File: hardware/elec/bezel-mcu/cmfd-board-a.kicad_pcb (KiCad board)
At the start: 2 copper layers, 140 x 140 mm, 37 parts, among them J1 B2B, J2 SWD, SW1 GAIN, SW2 SYM, SW3 BRT, SW4 CON, U1 STM32G431CBU6, U4 AMS1117-3.3

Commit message: feat(hardware): route Board A OSB 4x5 matrix to MCU
Add headless pcbnew matrix routing: ROW/COL nets, via-at-switch, B.Cu
buses, rocker nets, pin map. Export refreshed KiCad Gerbers and DRC.

Refs: #137
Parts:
- H1, H2, H3, H4: footprint MountingHole_3.2mm_M3_Pad -> MountingHole_3.2mm_M3
- moved H1 11.3 mm to (15.0, 15.0)
- moved H2 11.3 mm to (125.0, 15.0)
- moved H3 11.3 mm to (125.0, 125.0)
- moved H4 11.3 mm to (15.0, 125.0)
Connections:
- J1 pad 1: (no net) -> 3V3
- J1 pad 2: (no net) -> 3V3
- J1 pad 3: (no net) -> GND
- J1 pad 4: (no net) -> GND
- J1 pad 5: (no net) -> UART_TX
- J1 pad 6: (no net) -> UART_RX
- J2 pad 1: (no net) -> SWDIO
- J2 pad 2: (no net) -> SWCLK
- J2 pad 3: (no net) -> GND
- J2 pad 4: (no net) -> 3V3
- S1 pad 1: GND -> ROW_TOP
- S1 pad 2: GND -> COL0
- S10 pad 1: GND -> ROW_RIGHT
- S10 pad 2: GND -> COL4
- S11 pad 1: GND -> ROW_BOT
- S11 pad 2: GND -> COL4
- S12 pad 1: GND -> ROW_BOT
- S12 pad 2: GND -> COL3
- S13 pad 1: GND -> ROW_BOT
- S13 pad 2: GND -> COL2
- S14 pad 1: GND -> ROW_BOT
- S14 pad 2: GND -> COL1
- S15 pad 1: GND -> ROW_BOT
- S15 pad 2: GND -> COL0
- S16 pad 1: GND -> ROW_LEFT
- S16 pad 2: GND -> COL4
- S17 pad 1: GND -> ROW_LEFT
- S17 pad 2: GND -> COL3
- S18 pad 1: GND -> ROW_LEFT
- S18 pad 2: GND -> COL2
- S19 pad 1: GND -> ROW_LEFT
- S19 pad 2: GND -> COL1
- S2 pad 1: GND -> ROW_TOP
- S2 pad 2: GND -> COL1
- S20 pad 1: GND -> ROW_LEFT
- S20 pad 2: GND -> COL0
- S3 pad 1: GND -> ROW_TOP
- S3 pad 2: GND -> COL2
- S4 pad 1: GND -> ROW_TOP
- S4 pad 2: GND -> COL3
- S5 pad 1: GND -> ROW_TOP
- S5 pad 2: GND -> COL4
- S6 pad 1: GND -> ROW_RIGHT
- S6 pad 2: GND -> COL0
- S7 pad 1: GND -> ROW_RIGHT
- S7 pad 2: GND -> COL1
- S8 pad 1: GND -> ROW_RIGHT
- S8 pad 2: GND -> COL2
- S9 pad 1: GND -> ROW_RIGHT
- S9 pad 2: GND -> COL3
- SW1 pad 1: (no net) -> RK_GAIN
- SW1 pad 2: (no net) -> GND
- SW2 pad 1: (no net) -> RK_SYM
- SW2 pad 2: (no net) -> GND
- SW3 pad 1: (no net) -> RK_BRT
- SW3 pad 2: (no net) -> GND
- SW4 pad 1: (no net) -> RK_CON
- SW4 pad 2: (no net) -> GND
- U1 pad 10: (no net) -> ROW_TOP
- U1 pad 11: (no net) -> ROW_RIGHT
- U1 pad 12: (no net) -> ROW_BOT
- U1 pad 13: (no net) -> ROW_LEFT
- U1 pad 14: (no net) -> COL0
- U1 pad 15: (no net) -> COL1
- U1 pad 16: (no net) -> COL2
- U1 pad 17: (no net) -> COL3
- U1 pad 18: (no net) -> COL4
- U1 pad 19: (no net) -> RK_GAIN
- U1 pad 20: (no net) -> RK_SYM
- U1 pad 21: (no net) -> RK_BRT
- U1 pad 22: (no net) -> RK_CON
- U1 pad 29: (no net) -> UART_TX
- U1 pad 30: (no net) -> UART_RX
- U1 pad 34: (no net) -> SWDIO
- U1 pad 37: (no net) -> SWCLK
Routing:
- net COL0: track 0.00 -> 571.0 mm, vias 0 -> 5
- net COL1: track 0.00 -> 533.4 mm, vias 0 -> 5
- net COL2: track 0.00 -> 505.3 mm, vias 0 -> 5
- net COL3: track 0.00 -> 476.8 mm, vias 0 -> 5
- net COL4: track 0.00 -> 448.0 mm, vias 0 -> 5
- net RK_SYM: track 0.00 -> 349.7 mm, vias 0 -> 2
- net ROW_TOP: track 0.00 -> 348.0 mm, vias 0 -> 6
- net ROW_RIGHT: track 0.00 -> 332.2 mm, vias 0 -> 6
- net RK_CON: track 0.00 -> 250.8 mm, vias 0 -> 2
- net ROW_LEFT: track 0.00 -> 231.2 mm, vias 0 -> 6
- net RK_GAIN: track 0.00 -> 223.4 mm, vias 0 -> 2
- net ROW_BOT: track 0.00 -> 216.2 mm, vias 0 -> 6
- net RK_BRT: track 0.00 -> 125.0 mm, vias 0 -> 2
- net UART_RX: track 0.00 -> 53.2 mm
- net UART_TX: track 0.00 -> 50.2 mm
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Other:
- board text added: "MATRIX B.Cu bus + via-at-switch"

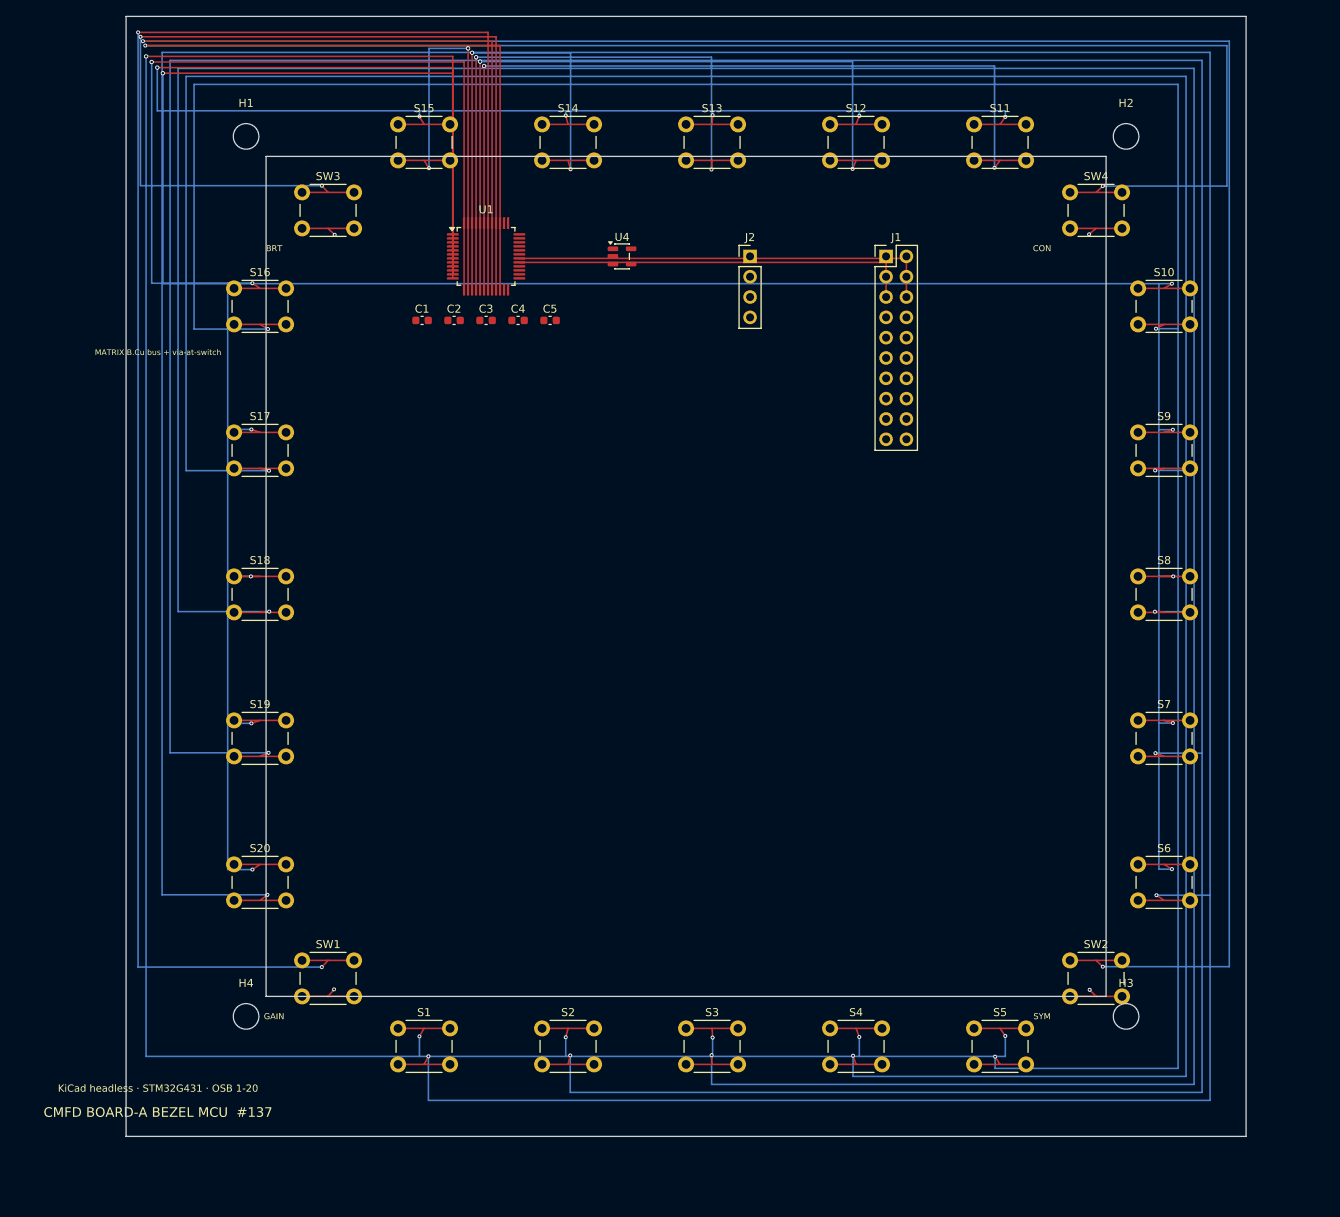
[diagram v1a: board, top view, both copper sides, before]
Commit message: feat(hardware): fab-ready passive bezel PCB + plain-language order guide
Board A is a switch-only panel: one pin per button, short tracks, zero
copper shorts on DRC. ORDER-THIS.md explains what to upload to JLCPCB and
the print shop with no KiCad steps.

Refs: #137
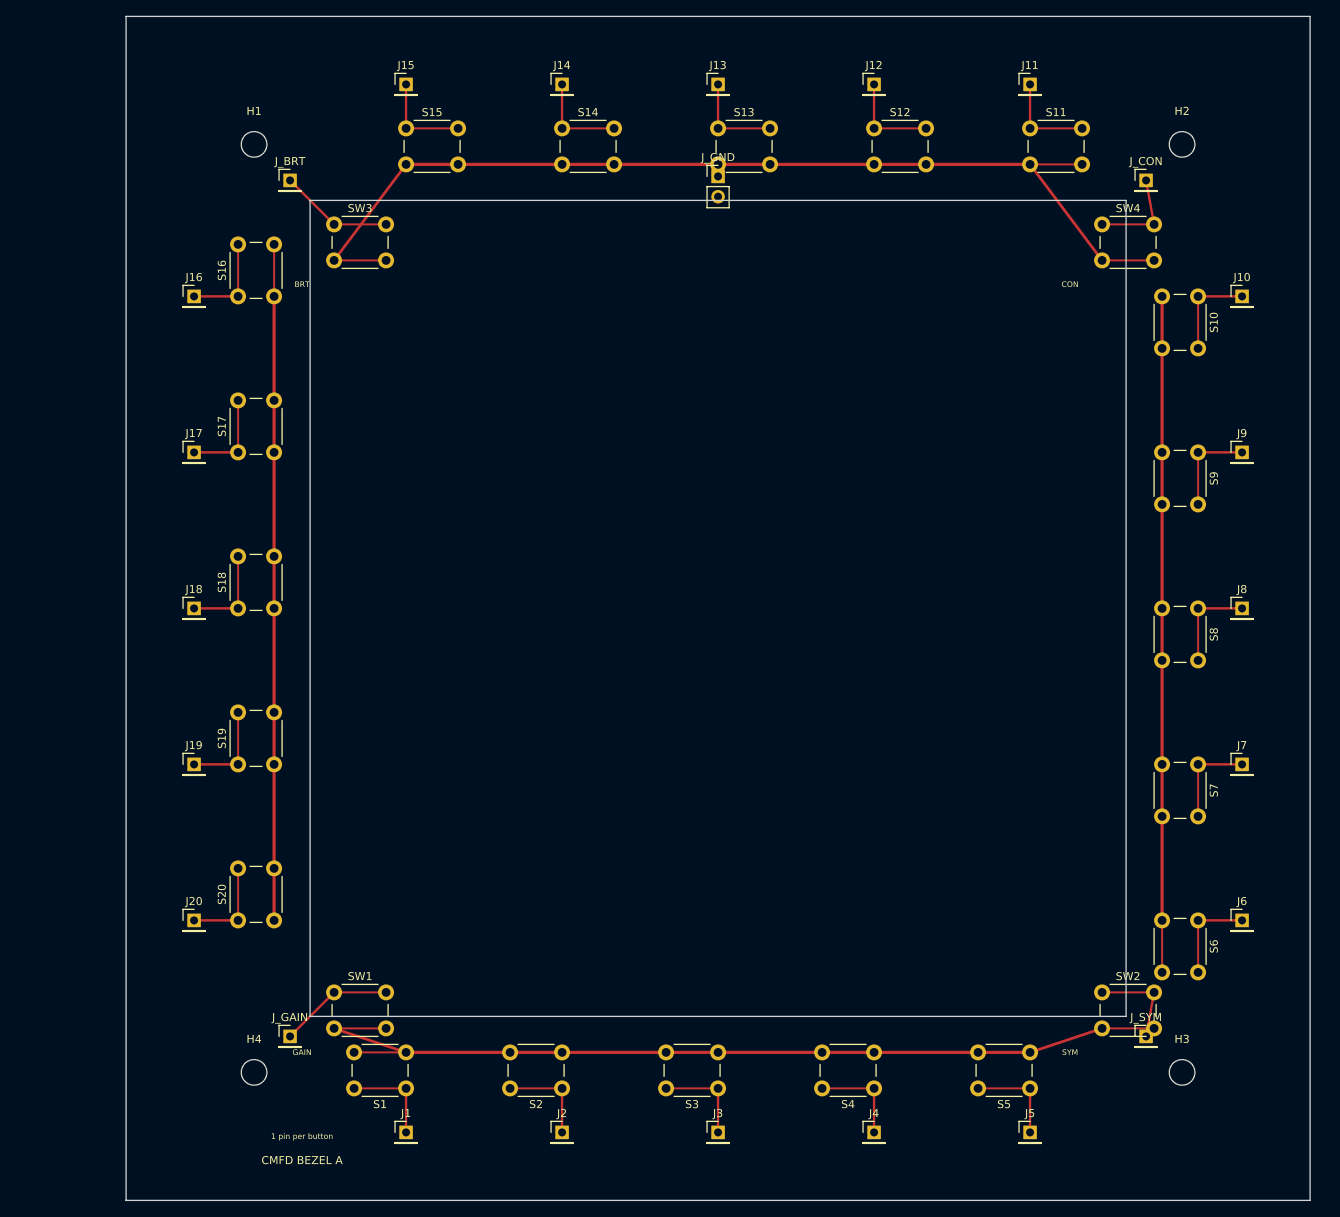
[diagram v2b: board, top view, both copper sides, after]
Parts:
- removed C1, C2, C3, C4, C5: 100nF, C_0603_1608Metric
- removed U1: STM32G431CBU6, LQFP-48_7x7mm_P0.5mm
- removed U4: AMS1117-3.3, SOT-23-5
- added J10: OSB10, PinHeader_1x01_P2.54mm_Vertical, F.Cu at (139.5, 35.0)
- added J11: OSB11, PinHeader_1x01_P2.54mm_Vertical, F.Cu at (113.0, 8.50)
- added J12: OSB12, PinHeader_1x01_P2.54mm_Vertical, F.Cu at (93.5, 8.50)
- added J13: OSB13, PinHeader_1x01_P2.54mm_Vertical, F.Cu at (74.0, 8.50)
- added J14: OSB14, PinHeader_1x01_P2.54mm_Vertical, F.Cu at (54.5, 8.50)
- added J15: OSB15, PinHeader_1x01_P2.54mm_Vertical, F.Cu at (35.0, 8.50)
- added J16: OSB16, PinHeader_1x01_P2.54mm_Vertical, F.Cu at (8.50, 35.0)
- added J17: OSB17, PinHeader_1x01_P2.54mm_Vertical, F.Cu at (8.50, 54.5)
- added J18: OSB18, PinHeader_1x01_P2.54mm_Vertical, F.Cu at (8.50, 74.0)
- added J19: OSB19, PinHeader_1x01_P2.54mm_Vertical, F.Cu at (8.50, 93.5)
- added J20: OSB20, PinHeader_1x01_P2.54mm_Vertical, F.Cu at (8.50, 113.0)
- added J3: OSB3, PinHeader_1x01_P2.54mm_Vertical, F.Cu at (74.0, 139.5)
- added J4: OSB4, PinHeader_1x01_P2.54mm_Vertical, F.Cu at (93.5, 139.5)
- added J5: OSB5, PinHeader_1x01_P2.54mm_Vertical, F.Cu at (113.0, 139.5)
- added J6: OSB6, PinHeader_1x01_P2.54mm_Vertical, F.Cu at (139.5, 113.0)
- added J7: OSB7, PinHeader_1x01_P2.54mm_Vertical, F.Cu at (139.5, 93.5)
- added J8: OSB8, PinHeader_1x01_P2.54mm_Vertical, F.Cu at (139.5, 74.0)
- added J9: OSB9, PinHeader_1x01_P2.54mm_Vertical, F.Cu at (139.5, 54.5)
- added J_BRT: BRT, PinHeader_1x01_P2.54mm_Vertical, F.Cu at (20.5, 20.5)
- added J_CON: CON, PinHeader_1x01_P2.54mm_Vertical, F.Cu at (127.5, 20.5)
- added J_GAIN: GAIN, PinHeader_1x01_P2.54mm_Vertical, F.Cu at (20.5, 127.5)
- added J_GND: GND, PinHeader_1x02_P2.54mm_Vertical, F.Cu at (74.0, 20.0)
- added J_SYM: SYM, PinHeader_1x01_P2.54mm_Vertical, F.Cu at (127.5, 127.5)
- J1: value B2B -> OSB1; footprint PinHeader_2x10_P2.54mm_Vertical -> PinHeader_1x01_P2.54mm_Vertical
- J2: value SWD -> OSB2; footprint PinHeader_1x04_P2.54mm_Vertical -> PinHeader_1x01_P2.54mm_Vertical
- moved J1 124.9 mm to (35.0, 139.5)
- moved J2 112.0 mm to (54.5, 139.5)
- moved S5 10.3 mm to (113.0, 134.0), turned to 180 degrees
- moved S6 10.3 mm to (134.0, 113.0), turned to -90 degrees
- moved H3 9.90 mm to (132.0, 132.0)
- moved S4 9.30 mm to (93.5, 134.0), turned to 180 degrees
- moved S7 9.30 mm to (134.0, 93.5), turned to -90 degrees
- moved S3 8.50 mm to (74.0, 134.0), turned to 180 degrees
- moved S8 8.50 mm to (134.0, 74.0), turned to -90 degrees
- moved S2 7.91 mm to (54.5, 134.0), turned to 180 degrees
- moved S9 7.91 mm to (134.0, 54.5), turned to -90 degrees
- moved S1 7.57 mm to (35.0, 134.0), turned to 180 degrees
- moved S10 7.57 mm to (134.0, 35.0), turned to -90 degrees
- moved H2 7.07 mm to (132.0, 16.0)
- moved H4 7.07 mm to (16.0, 132.0)
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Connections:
- J1 pad 1: 3V3 -> OSB1
- J2 pad 1: SWDIO -> OSB2
- S1 pad 1: ROW_TOP -> OSB1
- S1 pad 2: COL0 -> GND
- S10 pad 1: ROW_RIGHT -> OSB10
- S10 pad 2: COL4 -> GND
- S11 pad 1: ROW_BOT -> OSB11
- S11 pad 2: COL4 -> GND
- S12 pad 1: ROW_BOT -> OSB12
- S12 pad 2: COL3 -> GND
- S13 pad 1: ROW_BOT -> OSB13
- S13 pad 2: COL2 -> GND
- S14 pad 1: ROW_BOT -> OSB14
- S14 pad 2: COL1 -> GND
- S15 pad 1: ROW_BOT -> OSB15
- S15 pad 2: COL0 -> GND
- S16 pad 1: ROW_LEFT -> OSB16
- S16 pad 2: COL4 -> GND
- S17 pad 1: ROW_LEFT -> OSB17
- S17 pad 2: COL3 -> GND
- S18 pad 1: ROW_LEFT -> OSB18
- S18 pad 2: COL2 -> GND
- S19 pad 1: ROW_LEFT -> OSB19
- S19 pad 2: COL1 -> GND
- S2 pad 1: ROW_TOP -> OSB2
- S2 pad 2: COL1 -> GND
- S20 pad 1: ROW_LEFT -> OSB20
- S20 pad 2: COL0 -> GND
- S3 pad 1: ROW_TOP -> OSB3
- S3 pad 2: COL2 -> GND
- S4 pad 1: ROW_TOP -> OSB4
- S4 pad 2: COL3 -> GND
- S5 pad 1: ROW_TOP -> OSB5
- S5 pad 2: COL4 -> GND
- S6 pad 1: ROW_RIGHT -> OSB6
- S6 pad 2: COL0 -> GND
- S7 pad 1: ROW_RIGHT -> OSB7
- S7 pad 2: COL1 -> GND
- S8 pad 1: ROW_RIGHT -> OSB8
- S8 pad 2: COL2 -> GND
- S9 pad 1: ROW_RIGHT -> OSB9
- S9 pad 2: COL3 -> GND
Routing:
- net COL0: track 571.0 -> 0.00 mm, vias 5 -> 0
- net COL1: track 533.4 -> 0.00 mm, vias 5 -> 0
- net COL2: track 505.3 -> 0.00 mm, vias 5 -> 0
- net GND: track 30.6 -> 518.5 mm, vias 4 -> 0
- net COL3: track 476.8 -> 0.00 mm, vias 5 -> 0
- net COL4: track 448.0 -> 0.00 mm, vias 5 -> 0
- net ROW_TOP: track 348.0 -> 0.00 mm, vias 6 -> 0
- net RK_SYM: track 349.7 -> 12.1 mm, vias 2 -> 0
- net ROW_RIGHT: track 332.2 -> 0.00 mm, vias 6 -> 0
- net RK_CON: track 250.8 -> 12.1 mm, vias 2 -> 0
- net ROW_LEFT: track 231.2 -> 0.00 mm, vias 6 -> 0
- net ROW_BOT: track 216.2 -> 0.00 mm, vias 6 -> 0
- net RK_GAIN: track 223.4 -> 14.3 mm, vias 2 -> 0
- net RK_BRT: track 125.0 -> 14.3 mm, vias 2 -> 0
- net UART_RX: track 53.2 -> 0.00 mm
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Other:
- board size 140 x 140 mm -> 148 x 148 mm
- board text added: "1 pin per button"
- board text added: "CMFD BEZEL A"
- board text removed: "CMFD BOARD-A BEZEL MCU #137"
- board text removed: "KiCad headless · STM32G431 · OSB 1-20"
- board text removed: "MATRIX B.Cu bus + via-at-switch"

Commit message: fix(hardware): rockers clear glass, edge ports, M12, RA headers
- Rockers moved to pure corners (16 mm inset, 12×9 cap) so caps never
  enter the 102 mm glass aperture; OpenSCAD + KiCad + viewer aligned
- Board B USB-C / RJ45 / harness moved to front edge (not board center)
- Three M12 panel bulkheads on case left wall; J_M12 edge harness on B
- Board A uses right-angle 1-pin headers (outward); pins no longer
  taller than the 4.3 mm tact switches
- Rebuilt STLs, Gerbers, KiCad raytraces, Blender studio shots

Refs: #137
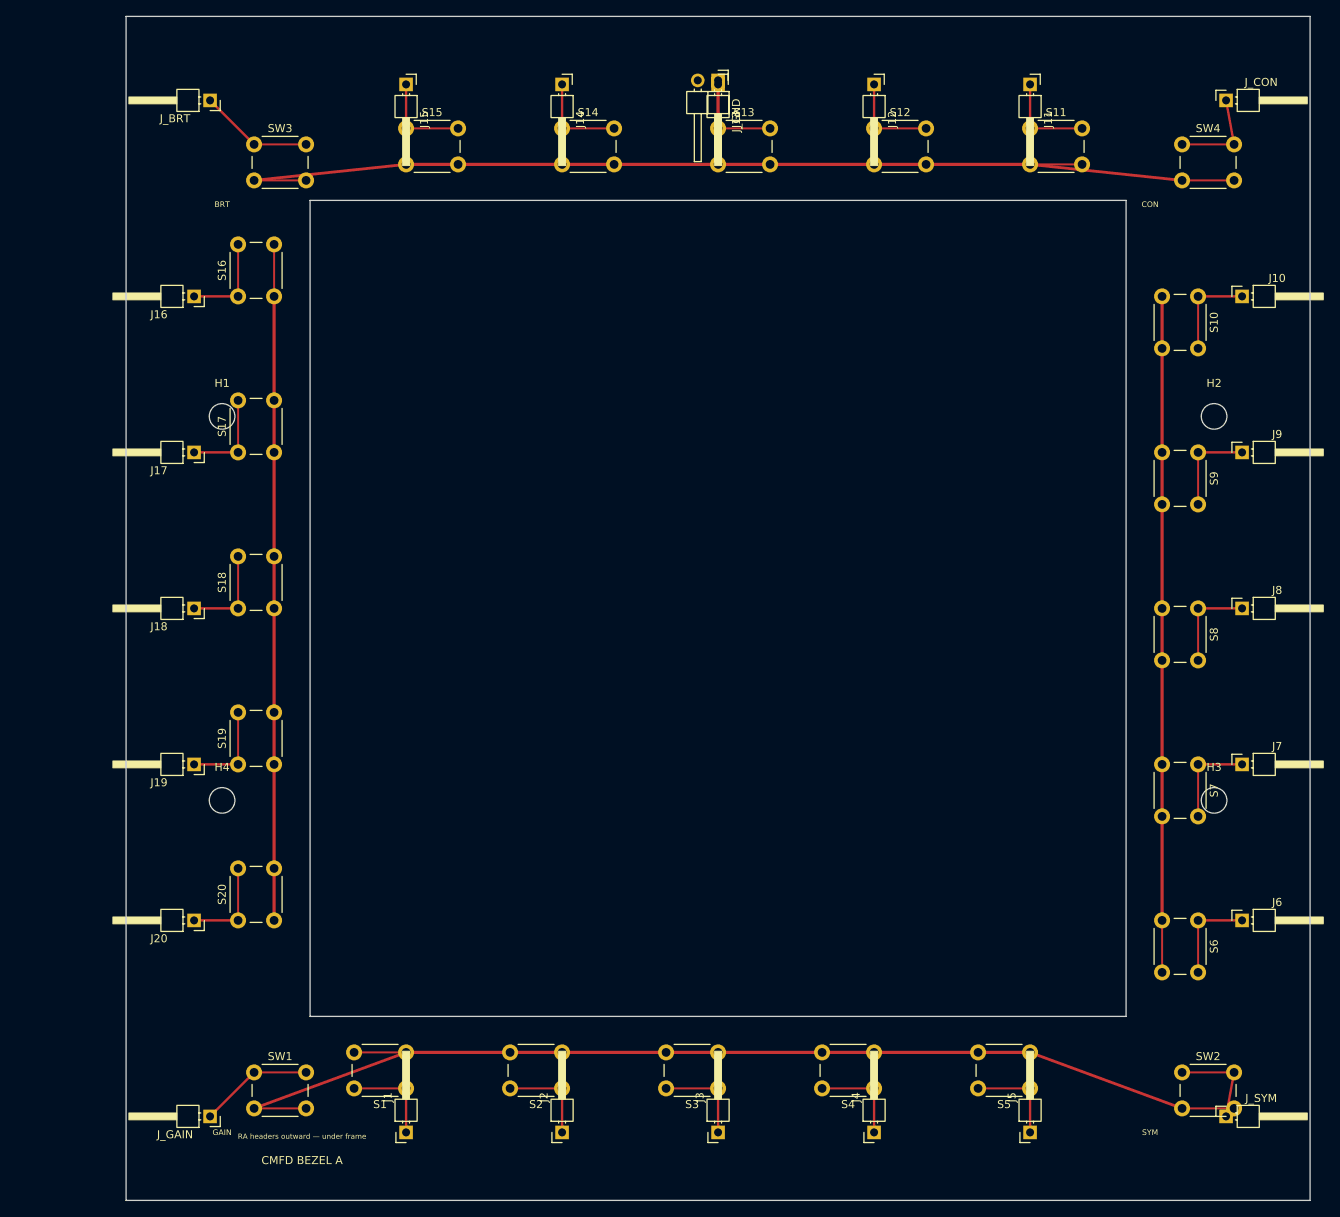
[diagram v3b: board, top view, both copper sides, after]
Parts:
- removed the J_BRT at (20.5, 20.5)
- removed the J_CON at (127.5, 20.5)
- removed the J_GAIN at (20.5, 127.5)
- removed the J_GND at (74.0, 20.0)
- removed the J_SYM at (127.5, 127.5)
- added J_BRT: BRT, PinHeader_1x01_P2.54mm_Horizontal, F.Cu at (10.5, 10.5)
- added J_CON: CON, PinHeader_1x01_P2.54mm_Horizontal, F.Cu at (137.5, 10.5)
- added J_GAIN: GAIN, PinHeader_1x01_P2.54mm_Horizontal, F.Cu at (10.5, 137.5)
- added J_GND: GND, PinHeader_1x02_P2.54mm_Horizontal, F.Cu at (74.0, 8.00)
- added J_SYM: SYM, PinHeader_1x01_P2.54mm_Horizontal, F.Cu at (137.5, 137.5)
- J1, J10, J11, J12, J13, J14, J15, J16, J17, J18, J19, J2, J20, J3, J4, J5, J6, J7, J8, J9: footprint PinHeader_1x01_P2.54mm_Vertical -> PinHeader_1x01_P2.54mm_Horizontal
- moved H1 34.2 mm to (12.0, 50.0)
- moved H2 34.2 mm to (136.0, 50.0)
- moved H3 34.2 mm to (136.0, 98.0)
- moved H4 34.2 mm to (12.0, 98.0)
- moved SW1 14.1 mm to (16.0, 132.0)
- moved SW2 14.1 mm to (132.0, 132.0)
- moved SW3 14.1 mm to (16.0, 16.0)
- moved SW4 14.1 mm to (132.0, 16.0)
- turned J1 to 90 degrees
- turned J11 to -90 degrees
- turned J12 to -90 degrees
- turned J13 to -90 degrees
- turned J14 to -90 degrees
- turned J15 to -90 degrees
- turned J16 to 180 degrees
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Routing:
- net GND: track 518.5 -> 557.2 mm
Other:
- board text added: "RA headers outward — under frame"
- board text removed: "1 pin per button"
